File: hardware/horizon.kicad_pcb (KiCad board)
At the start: 4 copper layers, 95 x 56.2 mm, 58 parts, among them J1 Conn_01x02_Pin, J2 Conn_01x06_Pin, J3 USB_C_Receptacle_USB2.0_14P, J4 Conn_01x14_Pin, J5 Conn_01x02_Socket, J6 Conn_01x02_Pin, Q1 NPN, SW1 SW_Push, SW2 SW_Push, U1 ESP32-S3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

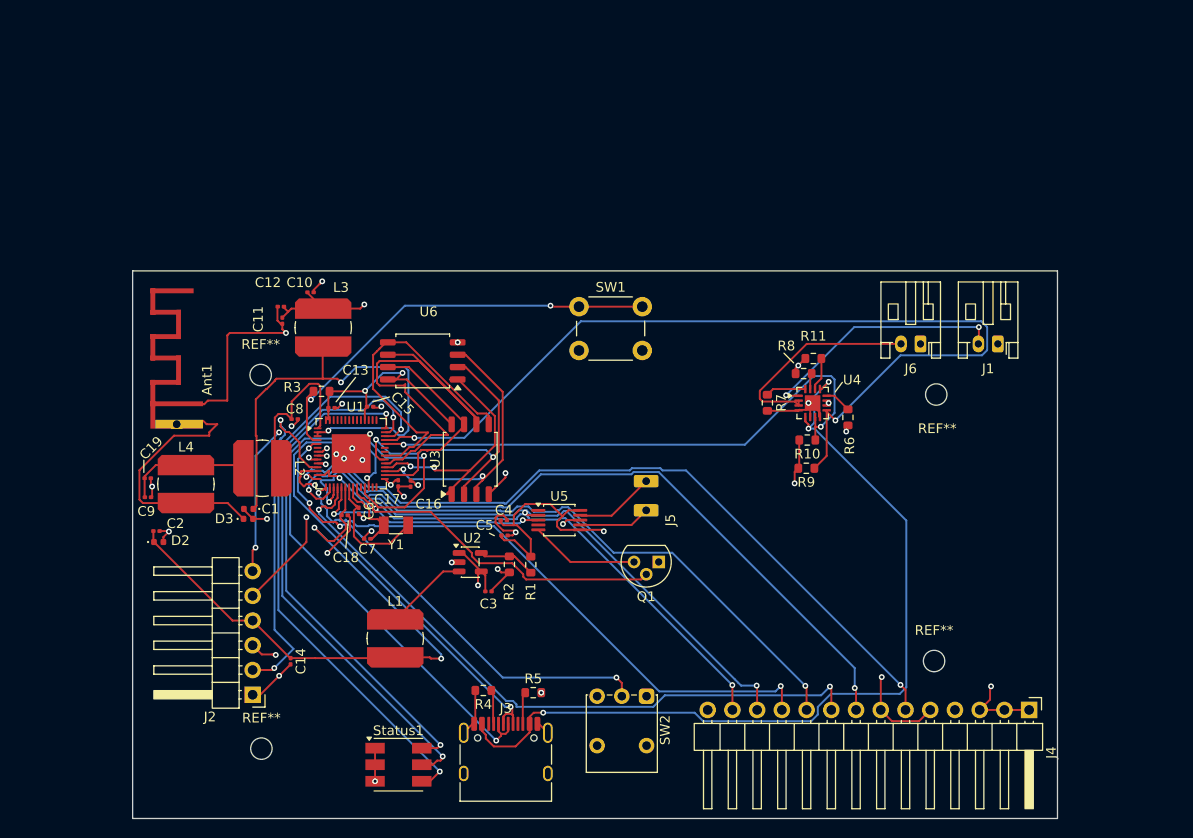
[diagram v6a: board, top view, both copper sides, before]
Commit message: Adding SD card slot
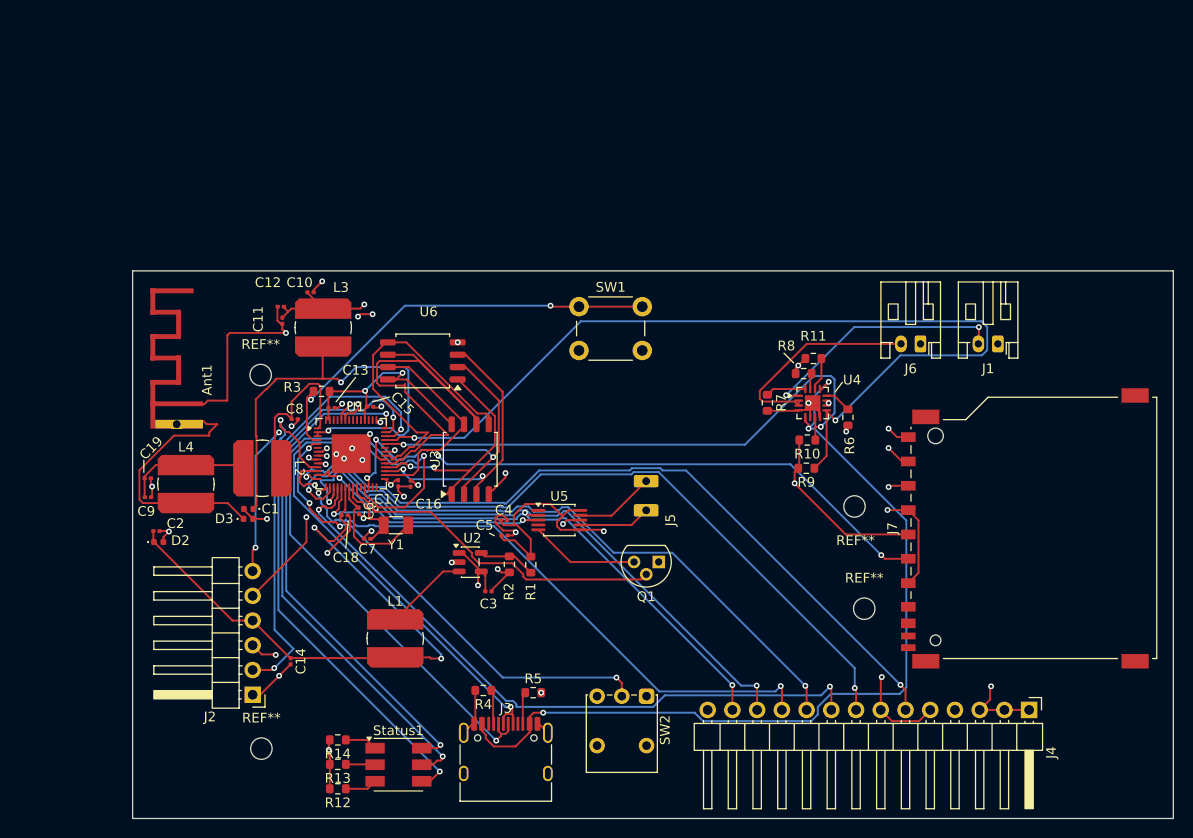
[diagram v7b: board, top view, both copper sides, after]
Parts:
- added J7: SD_Card_Receptacle, Connector_Card:SD_TE_2041021, F.Cu at (193.2, 77.2)
- added R12: 330Ω, Resistor_SMD:R_0603_1608Metric, F.Cu at (122.7, 104.0)
- added R13: 330Ω, Resistor_SMD:R_0603_1608Metric, F.Cu at (122.7, 101.5)
- added R14: 330Ω, Resistor_SMD:R_0603_1608Metric, F.Cu at (122.7, 99.0)
- moved REF** 14.2 mm to (175.8, 75.0)
- moved REF** 8.97 mm to (176.8, 85.5)
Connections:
- Status1 pad 1: GND -> Net-(Status1-RK)
- Status1 pad 2: GND -> Net-(Status1-GK)
- Status1 pad 3: GND -> Net-(Status1-BK)
- U1 pad 24: unconnected-(U1-GPIO18-Pad24) -> SDCARD_CD
- U1 pad 27: unconnected-(U1-GPIO21-Pad27) -> SDCARD_WP
- U1 pad 36: unconnected-(U1-SPICLK_N-Pad36) -> SDCARD_CLK
- U1 pad 37: unconnected-(U1-SPICLK_P-Pad37) -> SDCARD_SHELL
- U1 pad 43: unconnected-(U1-GPIO38-Pad43) -> SDCARD_CMD
- U1 pad 44: unconnected-(U1-MTCK-Pad44) -> SDCARD_DAT1
- U1 pad 51: unconnected-(U1-GPIO45-Pad51) -> SDCARD_DAT3
- U1 pad 52: unconnected-(U1-GPIO46-Pad52) -> SDCARD_DAT2
- U1 pad 6: unconnected-(U1-GPIO1-Pad6) -> SDCARD_DAT0
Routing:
- net SDCARD_DAT3: track 0.00 -> 95.5 mm, vias 0 -> 2
- net SDCARD_CMD: track 0.00 -> 78.3 mm, vias 0 -> 4
- net SDCARD_DAT2: track 0.00 -> 75.4 mm, vias 0 -> 2
- net SDCARD_CLK: track 0.00 -> 58.5 mm, vias 0 -> 3
- net VDD_SPI: track 251.5 -> 265.4 mm
- net GND: track 105.1 -> 118.2 mm, vias 30 -> 31
- net Net-(Status1-RK): track 0.00 -> 3.35 mm
- net Net-(Status1-BK): track 0.00 -> 3.32 mm
- net Net-(Status1-GK): track 0.00 -> 3.01 mm
- net USB_D-: track 68.4 -> 69.2 mm
- net QSPI_D0: track 32.6 -> 33.1 mm
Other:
- board size 95 x 56.2 mm -> 106.9 x 56.2 mm

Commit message: Finished SD card wiring
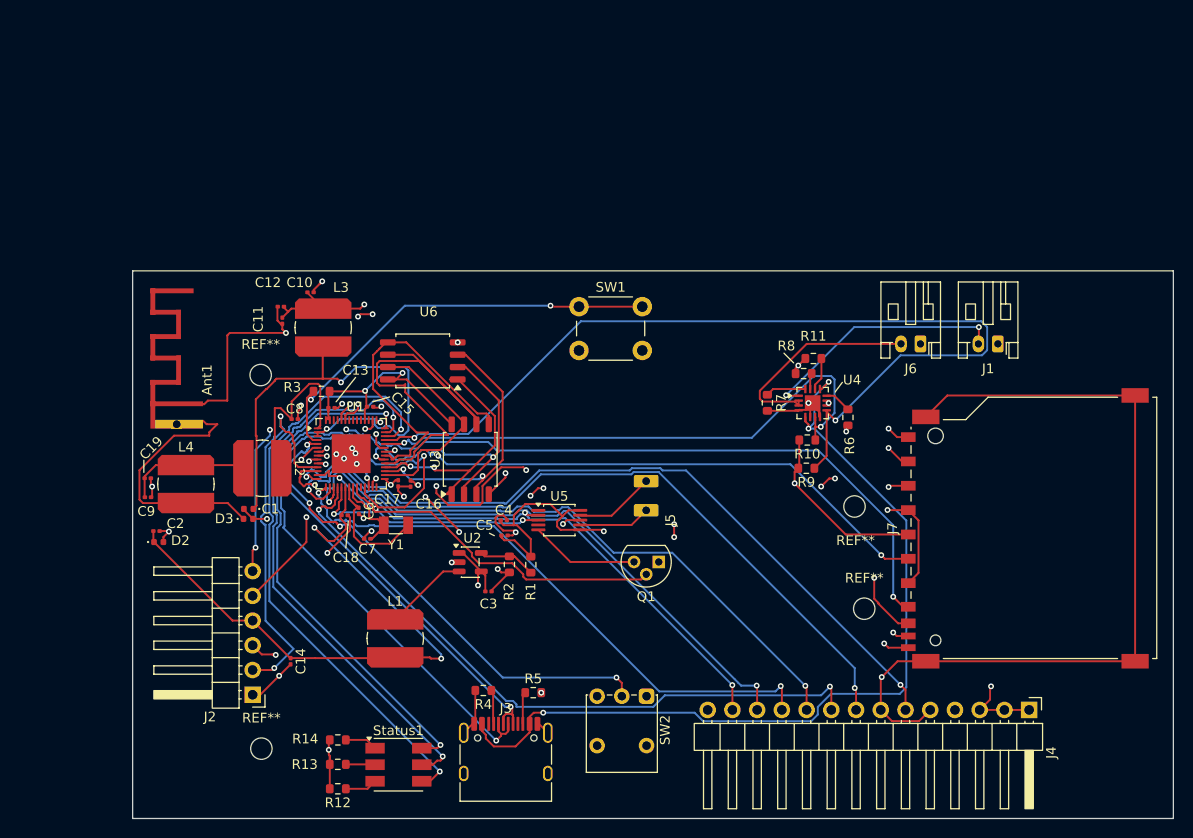
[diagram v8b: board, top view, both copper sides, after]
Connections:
- J7 pad SH: SDCARD_SHELL -> GND
- U1 pad 24: SDCARD_CD -> unconnected-(U1-GPIO18-Pad24)
- U1 pad 37: SDCARD_SHELL -> SDCARD_CD
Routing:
- net SDCARD_CD: track 0.00 -> 106.3 mm, vias 0 -> 6
- net SDCARD_DAT0: track 0.00 -> 78.5 mm, vias 0 -> 3
- net GND: track 118.2 -> 191.9 mm
- net SDCARD_DAT1: track 0.00 -> 68.9 mm, vias 0 -> 6
- net SDCARD_WP: track 0.00 -> 65.8 mm, vias 0 -> 4
- net +5V: track 108.8 -> 125.1 mm
- net Touch-SDA: track 20.7 -> 24.9 mm
- net Touch-INT: track 37.2 -> 40.1 mm
- net USB_D-: track 69.2 -> 71.9 mm
- net Net-(Status1-GA): track 57.6 -> 59.4 mm
- net Net-(Status1-BA): track 61.5 -> 63.2 mm
- net Net-(U1-GPIO0): track 49.3 -> 51.0 mm
- net Net-(Status1-RA): track 52.2 -> 53.9 mm
- net Net-(C1-Pad1): track 48.9 -> 50.3 mm
- net VDD_SPI: track 265.4 -> 266.7 mm
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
